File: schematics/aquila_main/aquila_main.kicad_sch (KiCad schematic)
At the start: 65 parts, among them IC1 TPS62152, IC2 TPS62132

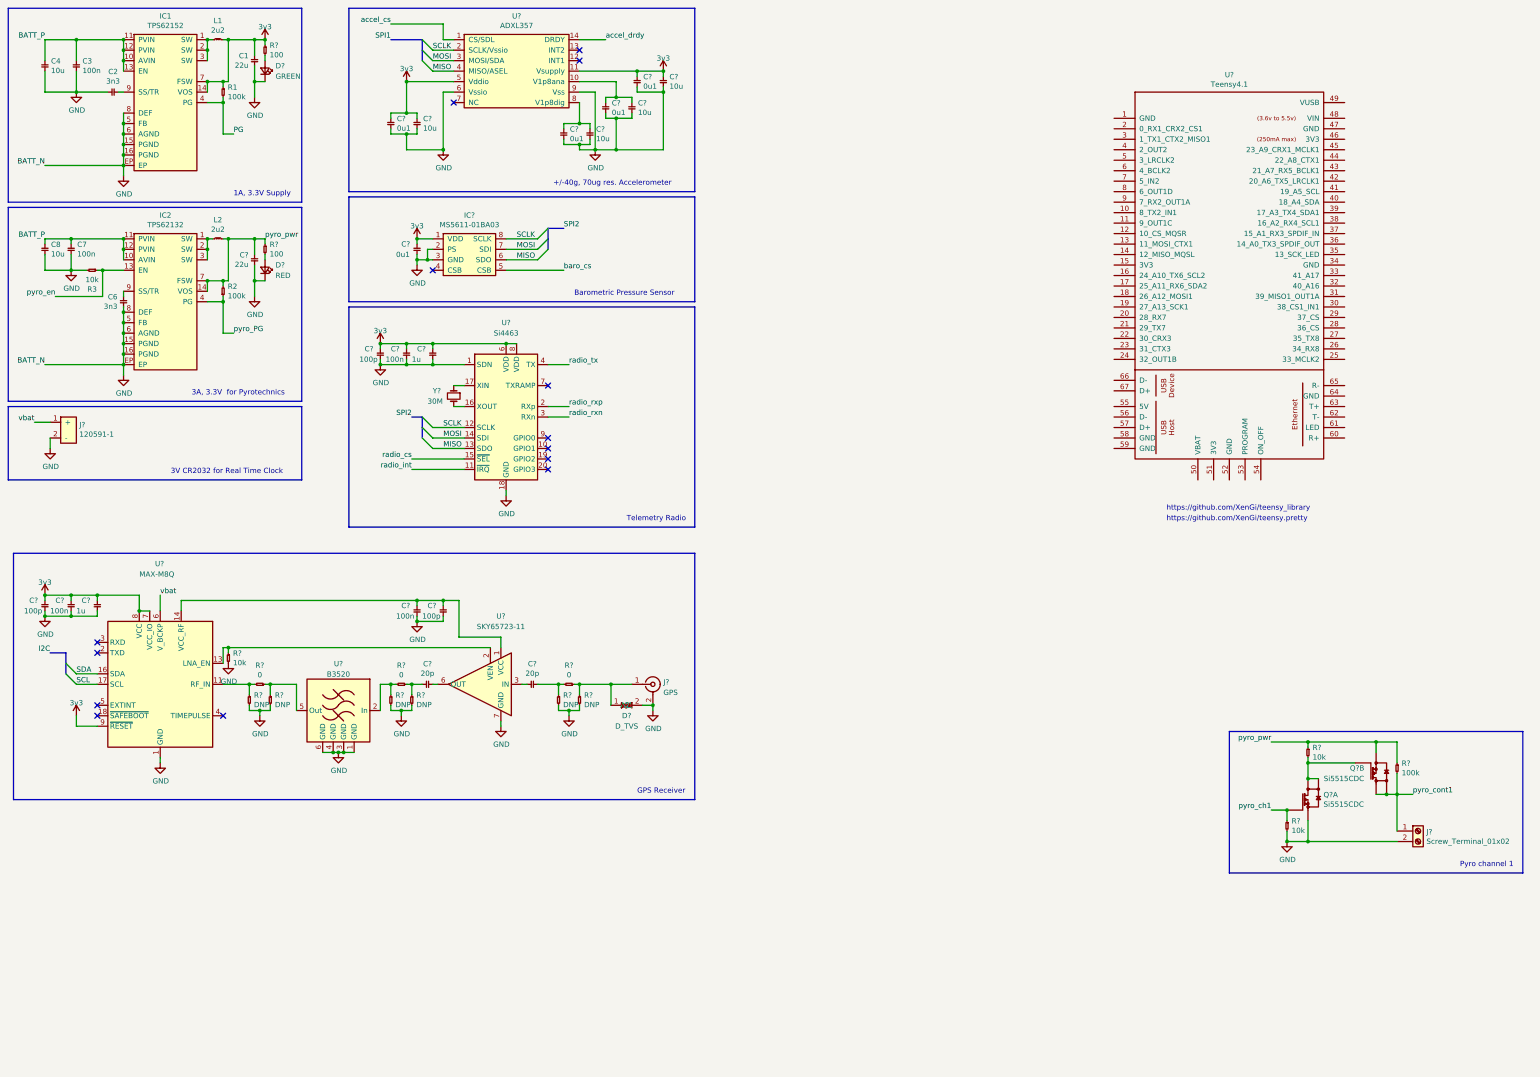
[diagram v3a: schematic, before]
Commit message: added battery holders and balancer
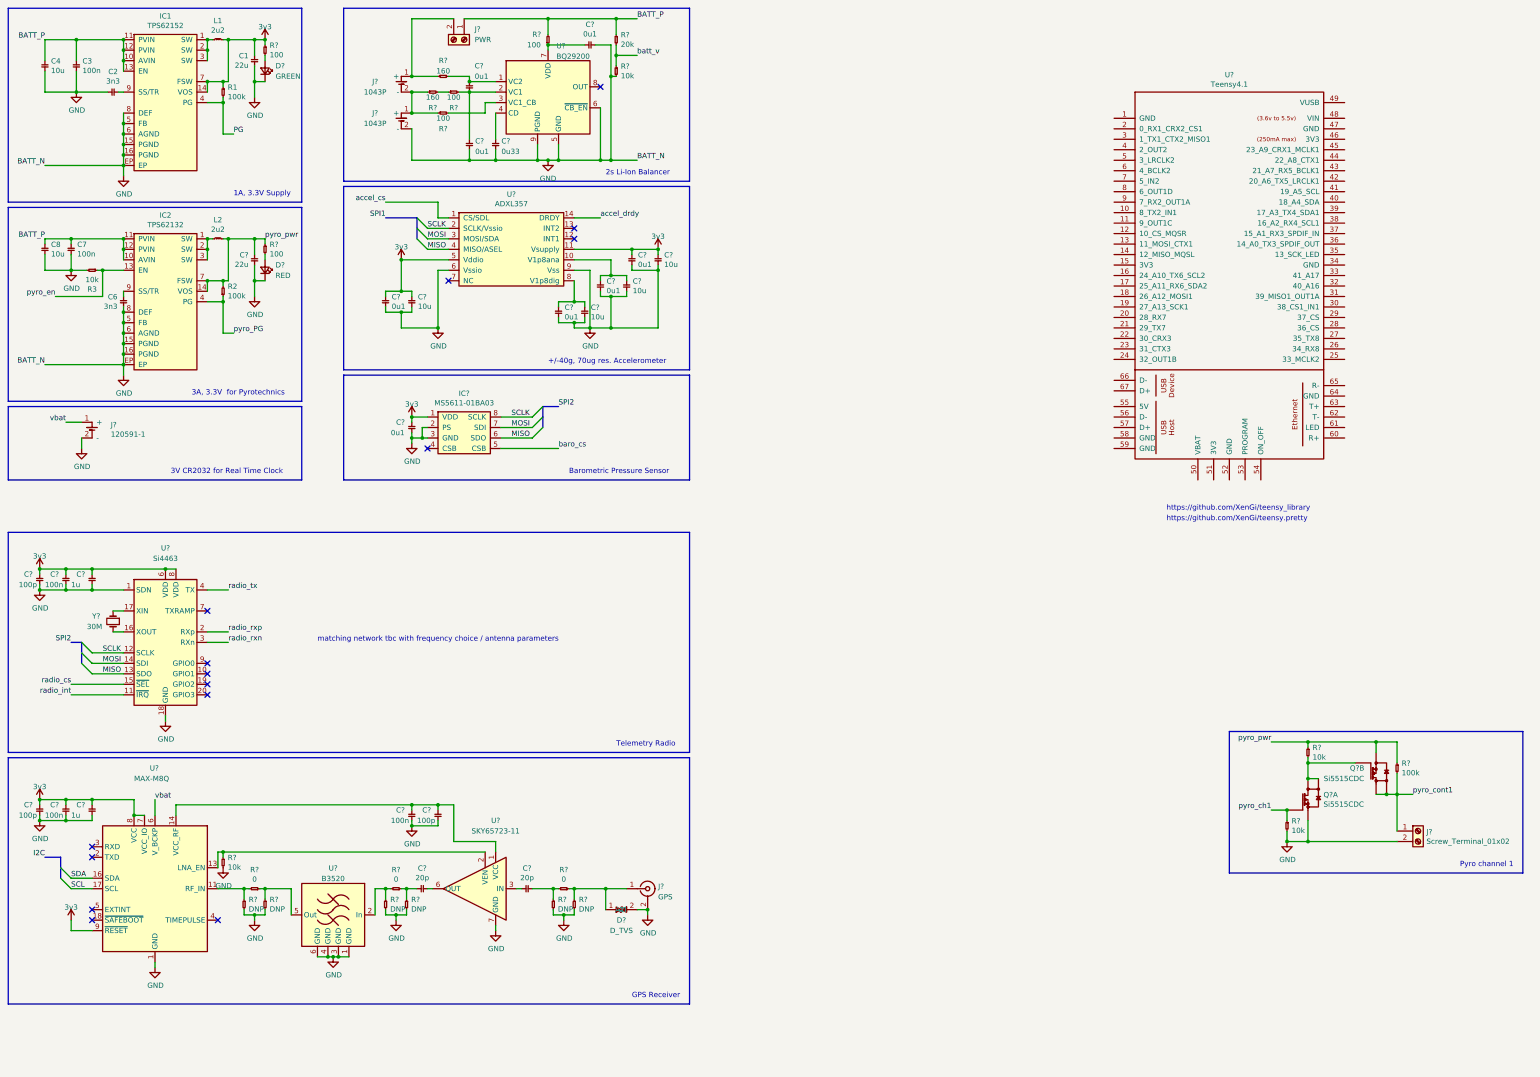
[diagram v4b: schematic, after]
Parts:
- added C?: 0u33, symbol aquila:C-cusf-kicad
- added C? (x3): 0u1, symbol aquila:C-cusf-kicad
- added J?: PWR, symbol Connector:Screw_Terminal_01x02
- added J? (x2): 1043P, aquila:1043, symbol aquila:1043P
- added R?: 10k, symbol aquila:R-cusf-kicad
- added R? (x3): 100, symbol aquila:R-cusf-kicad
- added R? (x2): 160, symbol aquila:R-cusf-kicad
- added R?: 20k, symbol aquila:R-cusf-kicad
- added U?: BQ29200, symbol aquila:BQ29200
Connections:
- net BATT_P: now also J?.1 (Pin_1), R?.1, R?.2
- net GND: now also C?.1, C?.1, C?.2, J?.2 (-), R?.2, U?.5 (GND), U?.6 (~{CB_EN}), U?.9 (PGND)
- new net: C?.2, R?.2, U?.1 (VC2)
- new net: C?.1, C?.2, R?.2, U?.2 (VC1)
- new net: R?.2, U?.3 (VC1_CB)
- new net: C?.2, U?.4 (CD)
- new net: C?.1, R?.1, U?.7 (VDD)
- new net: R?.1, R?.2
- new net: J?.1 (+), J?.2 (Pin_2), R?.1
- new net: J?.1 (+), J?.2 (-), R?.1, R?.1
- new net batt_v: R?.1, R?.2
- no-connect marks 14 -> 15
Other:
- note added: "2s Li-Ion Balancer"
- note added: "matching network tbc with frequency choice / antenna parameters"
- moved on the sheet: C?, D?, IC?, J?, R?, U?, Y?

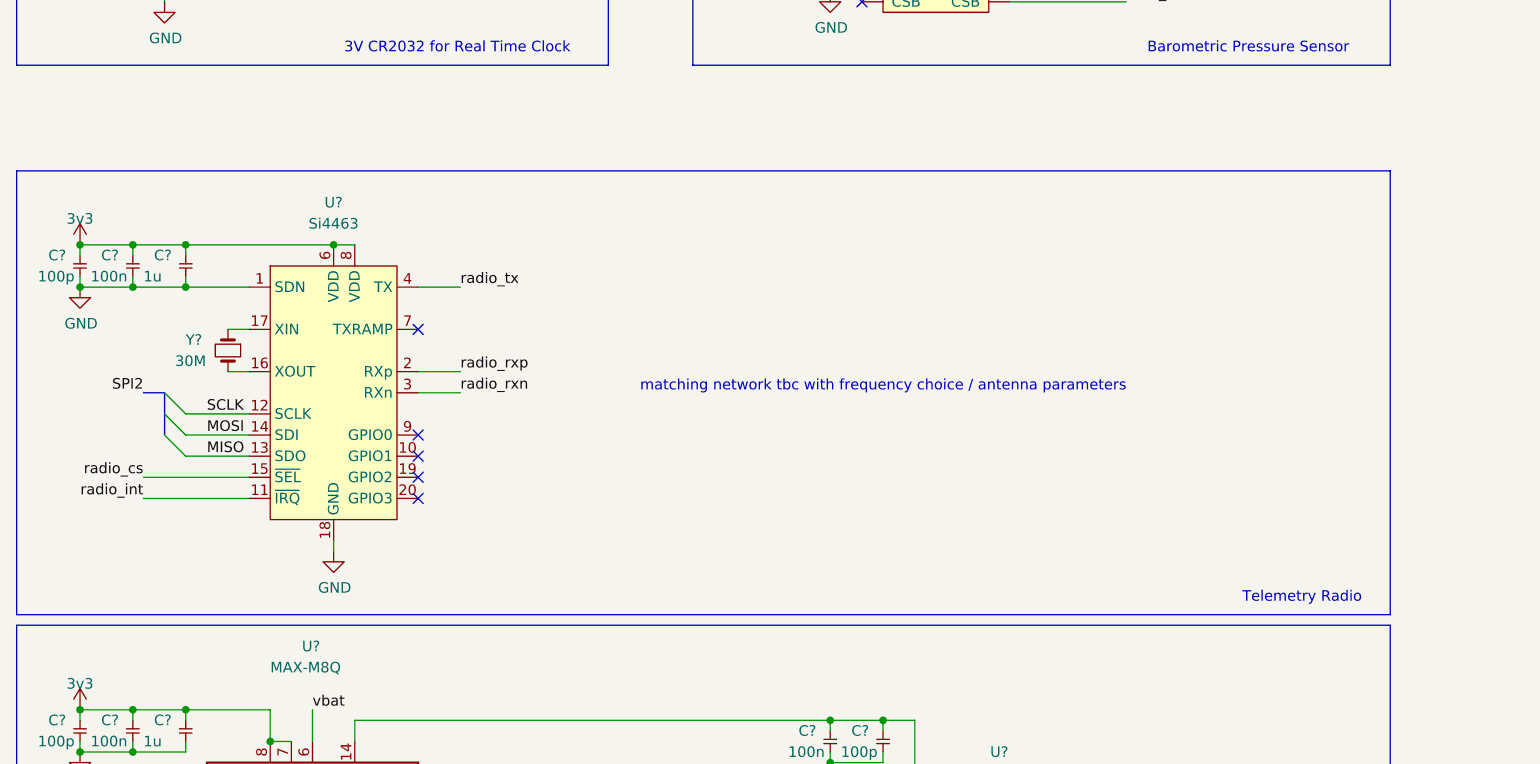
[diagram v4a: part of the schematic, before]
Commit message: added telemetry radio matching network
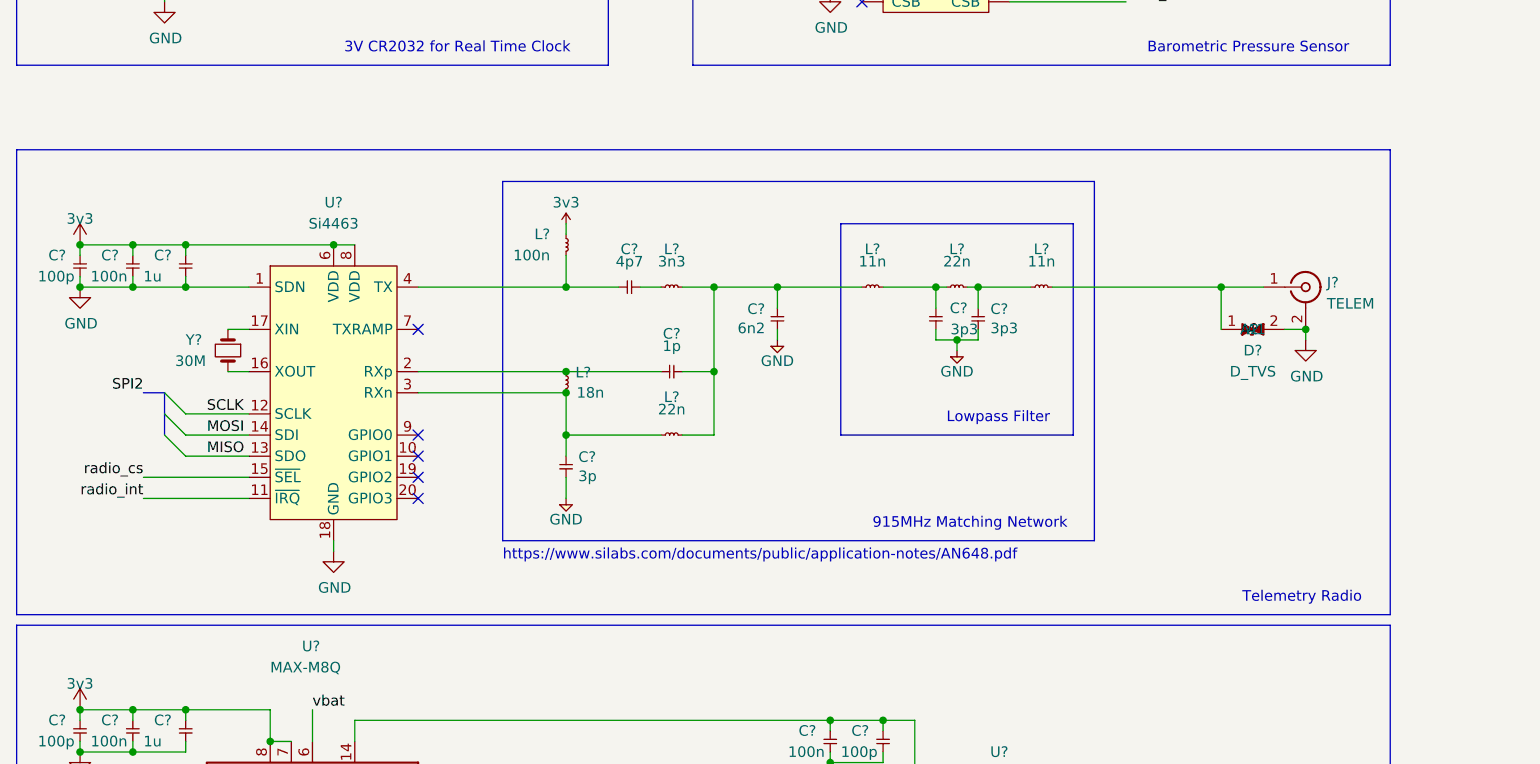
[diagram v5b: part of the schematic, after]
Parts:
- added C?: 1p, Strix:C_0402, symbol Strix:C
- added C? (x2): 3p3, Strix:C_0402, symbol Strix:C
- added C?: 6n2, Strix:C_0402, symbol Strix:C
- added C?: 3p, Strix:C_0402, symbol Strix:C
- added C?: 4p7, Strix:C_0402, symbol Strix:C
- added D?: D_TVS, symbol aquila:D_TVS
- added J?: TELEM, symbol Connector:Conn_Coaxial
- added L? (x2): 11n, Strix:L_0402, symbol Strix:L
- added L?: 18n, Strix:L_0402, symbol Strix:L
- added L?: 100n, Strix:L_0402, symbol Strix:L
- added L?: 3n3, Strix:L_0402, symbol Strix:L
- added L? (x2): 22n, Strix:L_0402, symbol Strix:L
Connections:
- net GND: now also C?.2, C?.2, C?.2, C?.2, D?.2 (A2), J?.2 (Ext)
- net radio_rxn: no longer names the net of U?.3 (RXn)
- net radio_rxn: now also C?.1, L?.1, L?.2
- net radio_rxp: no longer names the net of U?.2 (RXp)
- net radio_rxp: now also C?.1, L?.1
- net radio_tx: no longer names the net of U?.4 (TX)
- net radio_tx: now also C?.1, L?.2
- new net: C?.1, C?.2, L?.1, L?.2, L?.2
- new net: C?.1, L?.1, L?.2 (x2)
- new net: D?.1 (A1), J?.1 (In), L?.2
- new net: C?.2, L?.1
- new net 3v3: L?.1
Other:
- note added: "915MHz Matching Network"
- note added: "Lowpass Filter"
- note added: "https://www.silabs.com/documents/public/application-notes/AN648.pdf"
- note removed: "matching network tbc with frequency choice / antenna parameters"
